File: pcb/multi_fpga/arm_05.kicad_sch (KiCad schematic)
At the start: 16 parts, among them U41 IM72D128V01XTMA1, U42 IM72D128V01XTMA1, U43 IM72D128V01XTMA1, U44 IM72D128V01XTMA1, U45 IM72D128V01XTMA1, U46 IM72D128V01XTMA1, U47 IM72D128V01XTMA1, U48 IM72D128V01XTMA1

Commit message: Fixed library and power issues.
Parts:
- C41, C42, C43, C44, C45, C46, C47, C48: symbol C -> multi_fpga:C
- U41, U42, U43, U44, U45, U46, U47, U48: symbol IM72D128 -> multi_fpga:IM72D128

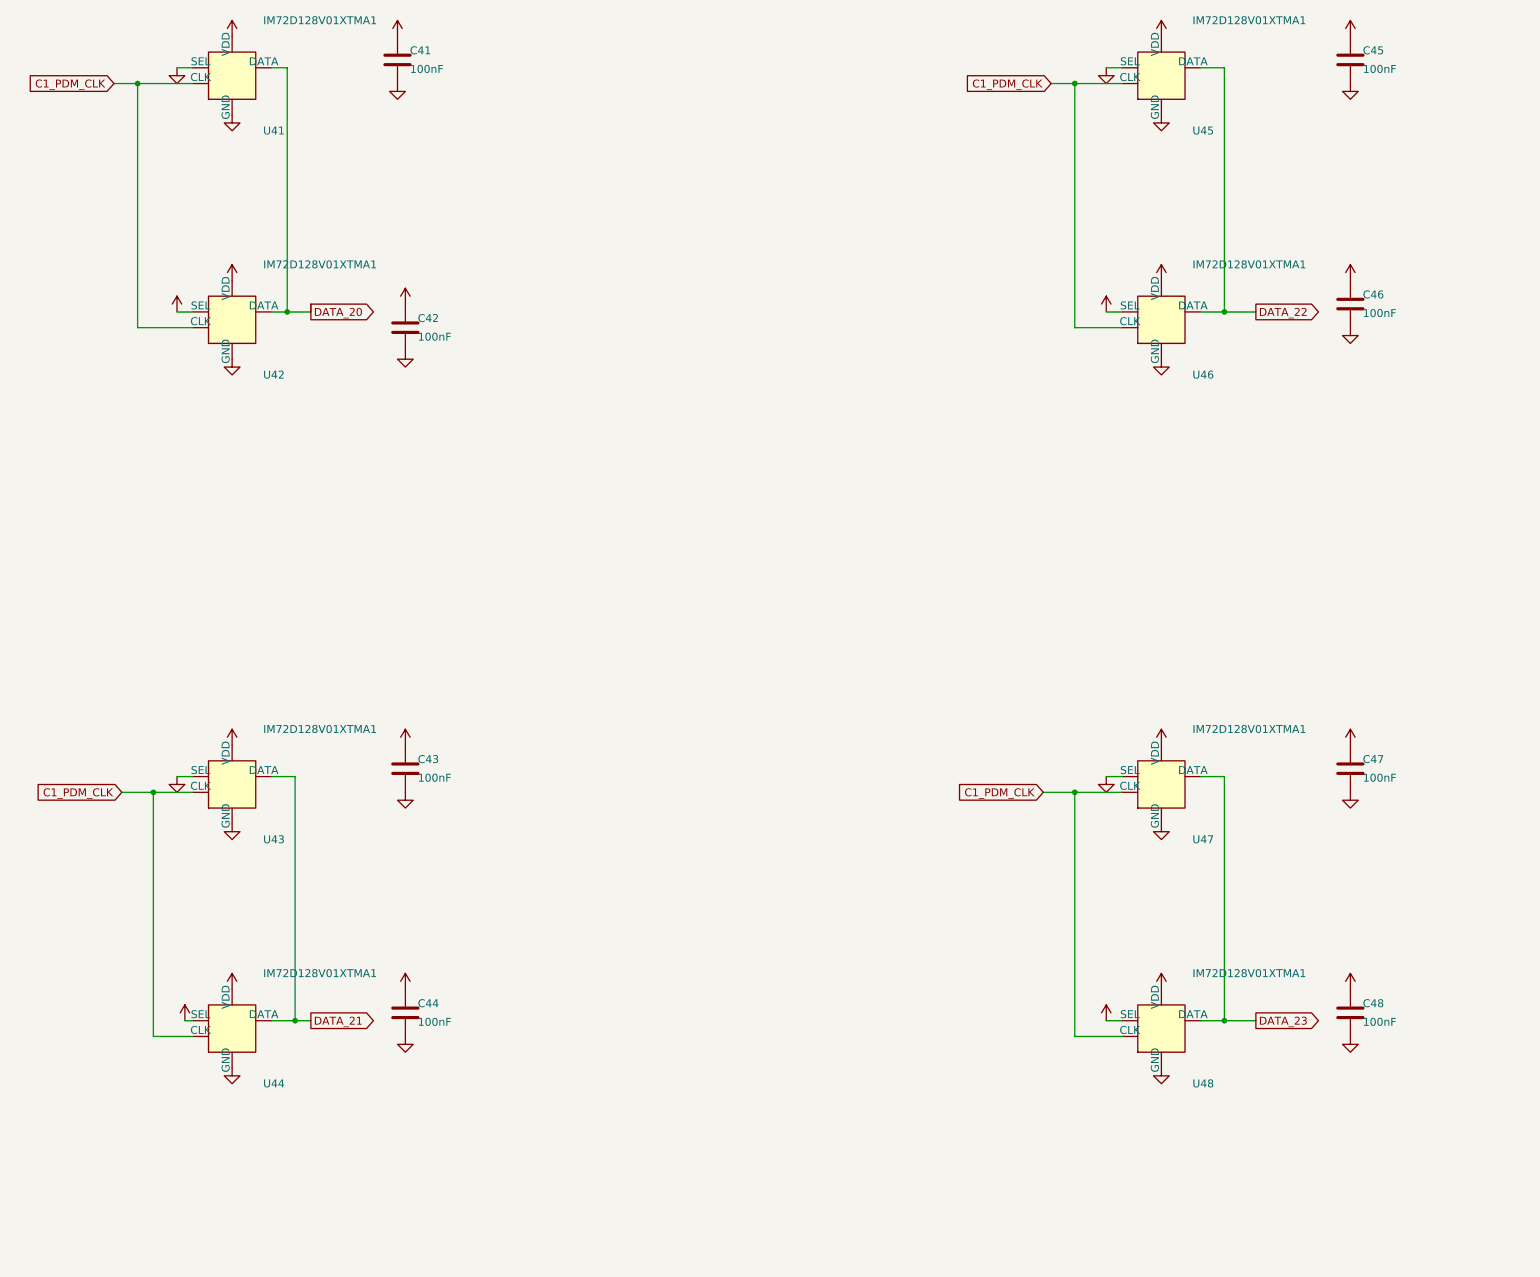
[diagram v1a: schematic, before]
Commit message: Fixed power and C ref des collisions.
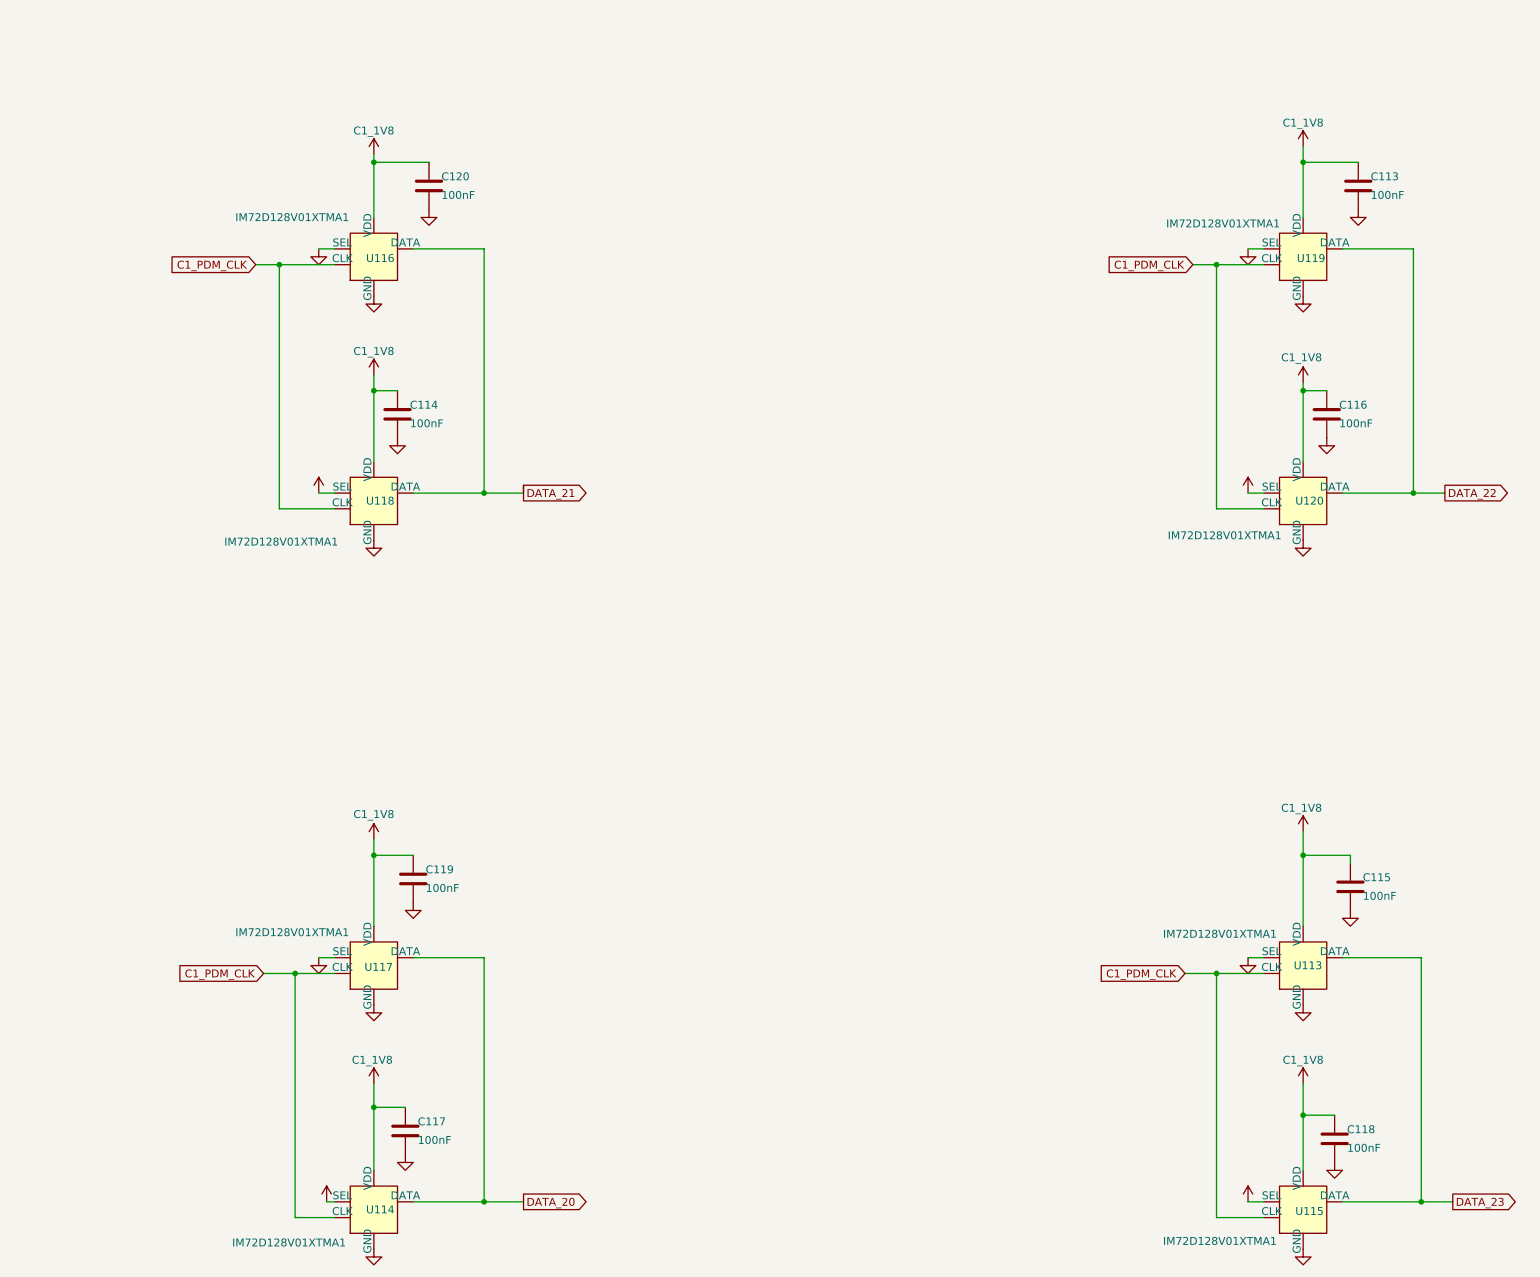
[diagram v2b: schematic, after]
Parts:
- removed C41, C42, C43, C44, C45, C46, C47, C48: 100nF, symbol multi_fpga:C
- removed U41, U42, U43, U44, U45, U46, U47, U48: IM72D128V01XTMA1, symbol multi_fpga:IM72D128
- added C113, C114, C115, C116, C117, C118, C119, C120: 100nF, symbol multi_fpga:C
- added U113, U114, U115, U116, U117, U118, U119, U120: IM72D128V01XTMA1, symbol multi_fpga:IM72D128
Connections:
- net C1_1V8: now also C113.1, C114.1, C115.1, C116.1, C117.1, C118.1, C119.1, C120.1, U113.2 (VDD), U114.2 (VDD), U114.4 (SEL), U115.2 (VDD), U115.4 (SEL), U116.2 (VDD), U117.2 (VDD), U118.2 (VDD), U118.4 (SEL), U119.2 (VDD), U120.2 (VDD), U120.4 (SEL)
- net C1_PDM_CLK: now also U113.3 (CLK), U114.3 (CLK), U115.3 (CLK), U116.3 (CLK), U117.3 (CLK), U118.3 (CLK), U119.3 (CLK), U120.3 (CLK)
- net DATA_20: now also U114.1 (DATA), U117.1 (DATA)
- net DATA_21: now also U116.1 (DATA), U118.1 (DATA)
- net DATA_22: now also U119.1 (DATA), U120.1 (DATA)
- net DATA_23: now also U113.1 (DATA), U115.1 (DATA)
- net GND: now also C113.2, C114.2, C115.2, C116.2, C117.2, C118.2, C119.2, C120.2, U113.4 (SEL), U113.5 (GND), U114.5 (GND), U115.5 (GND), U116.4 (SEL), U116.5 (GND), U117.4 (SEL), U117.5 (GND), U118.5 (GND), U119.4 (SEL), U119.5 (GND), U120.5 (GND)

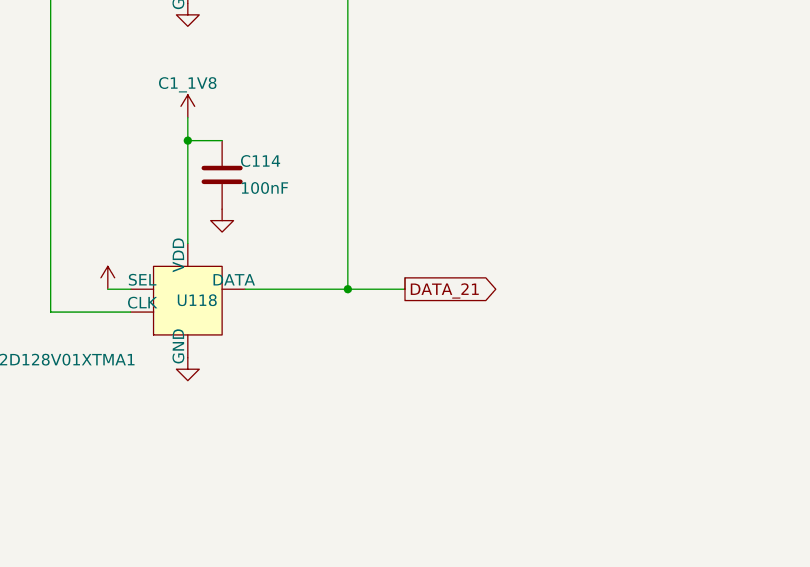
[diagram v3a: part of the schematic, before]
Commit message: Fixed regulator connection errors and dangling wire.
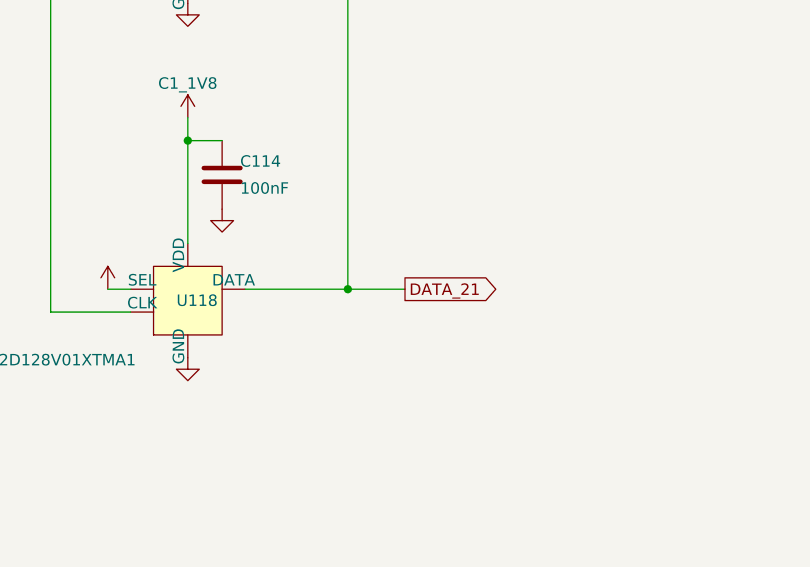
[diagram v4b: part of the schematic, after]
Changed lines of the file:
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@@
-	(wire
-		(pts
-			(xy 127 106.68) (xy 127 107.95)
-		)
-		(stroke
-			(width 0)
-			(type default)
-		)
-	)
 	(wire
 		(pts

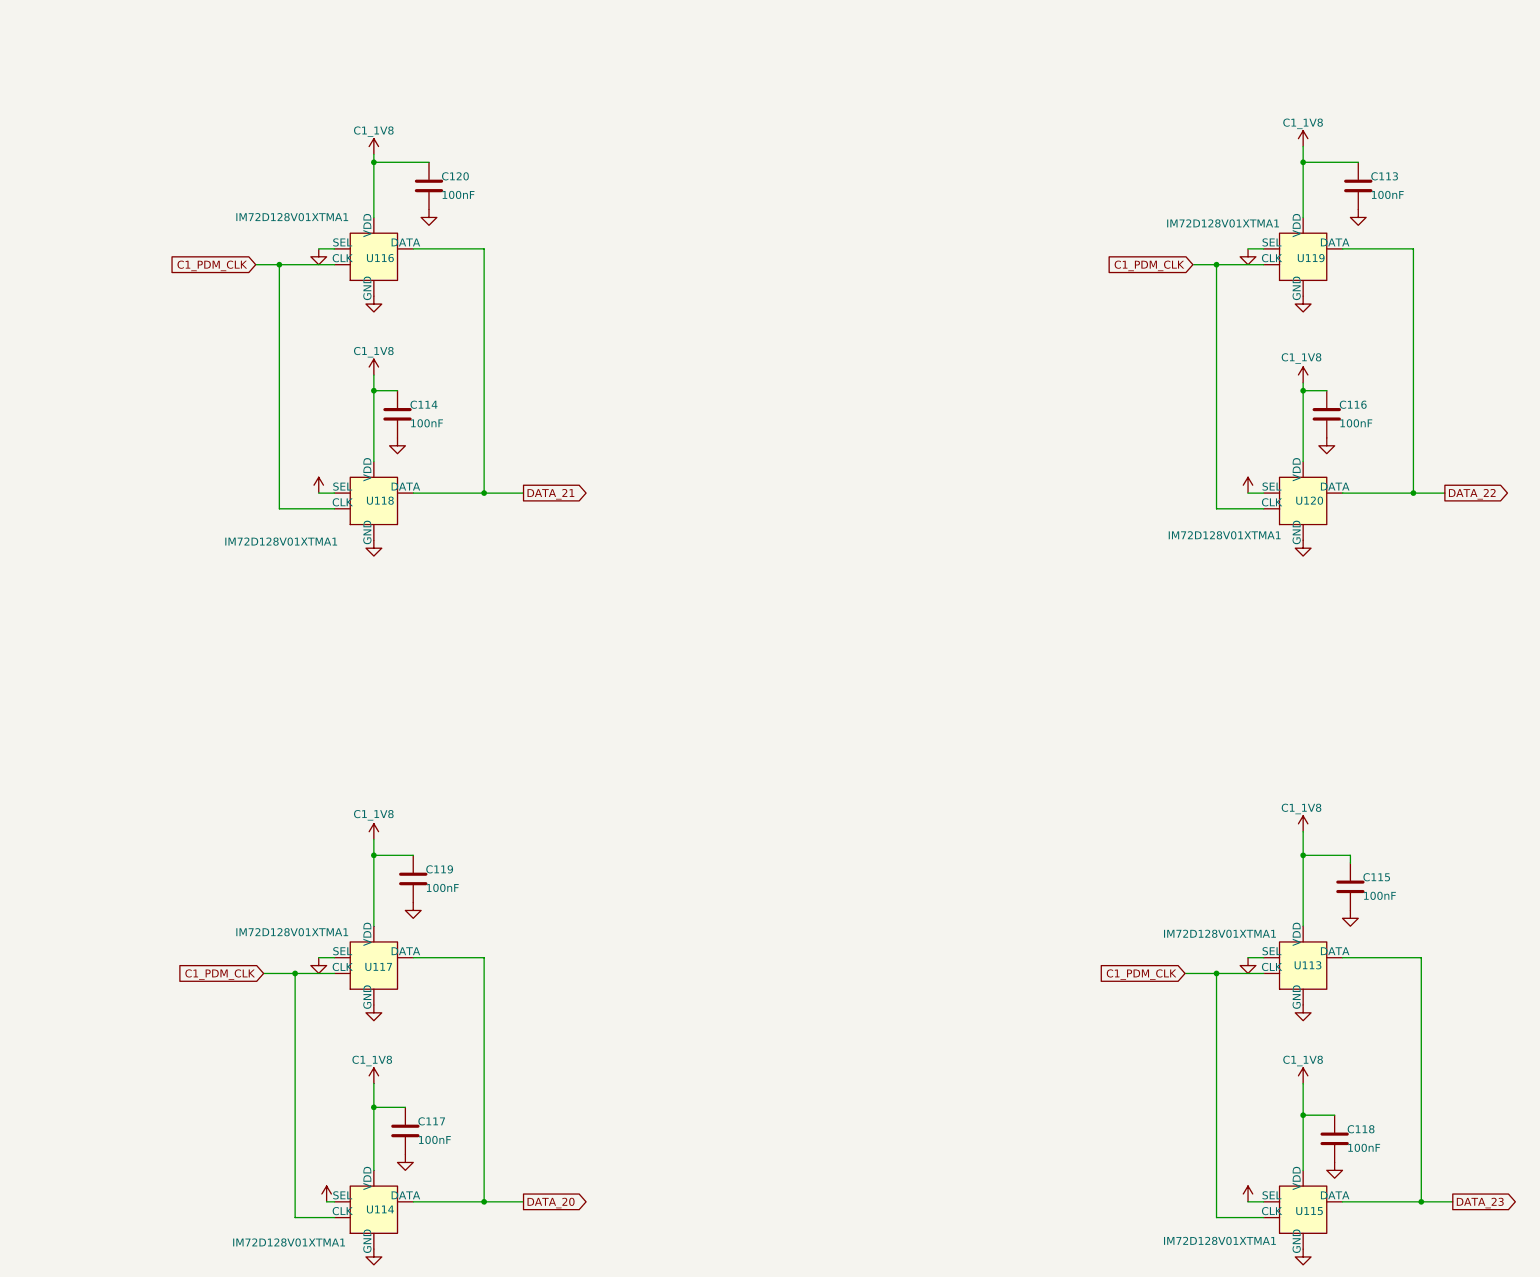
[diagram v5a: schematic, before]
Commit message: Global fix of res defs.
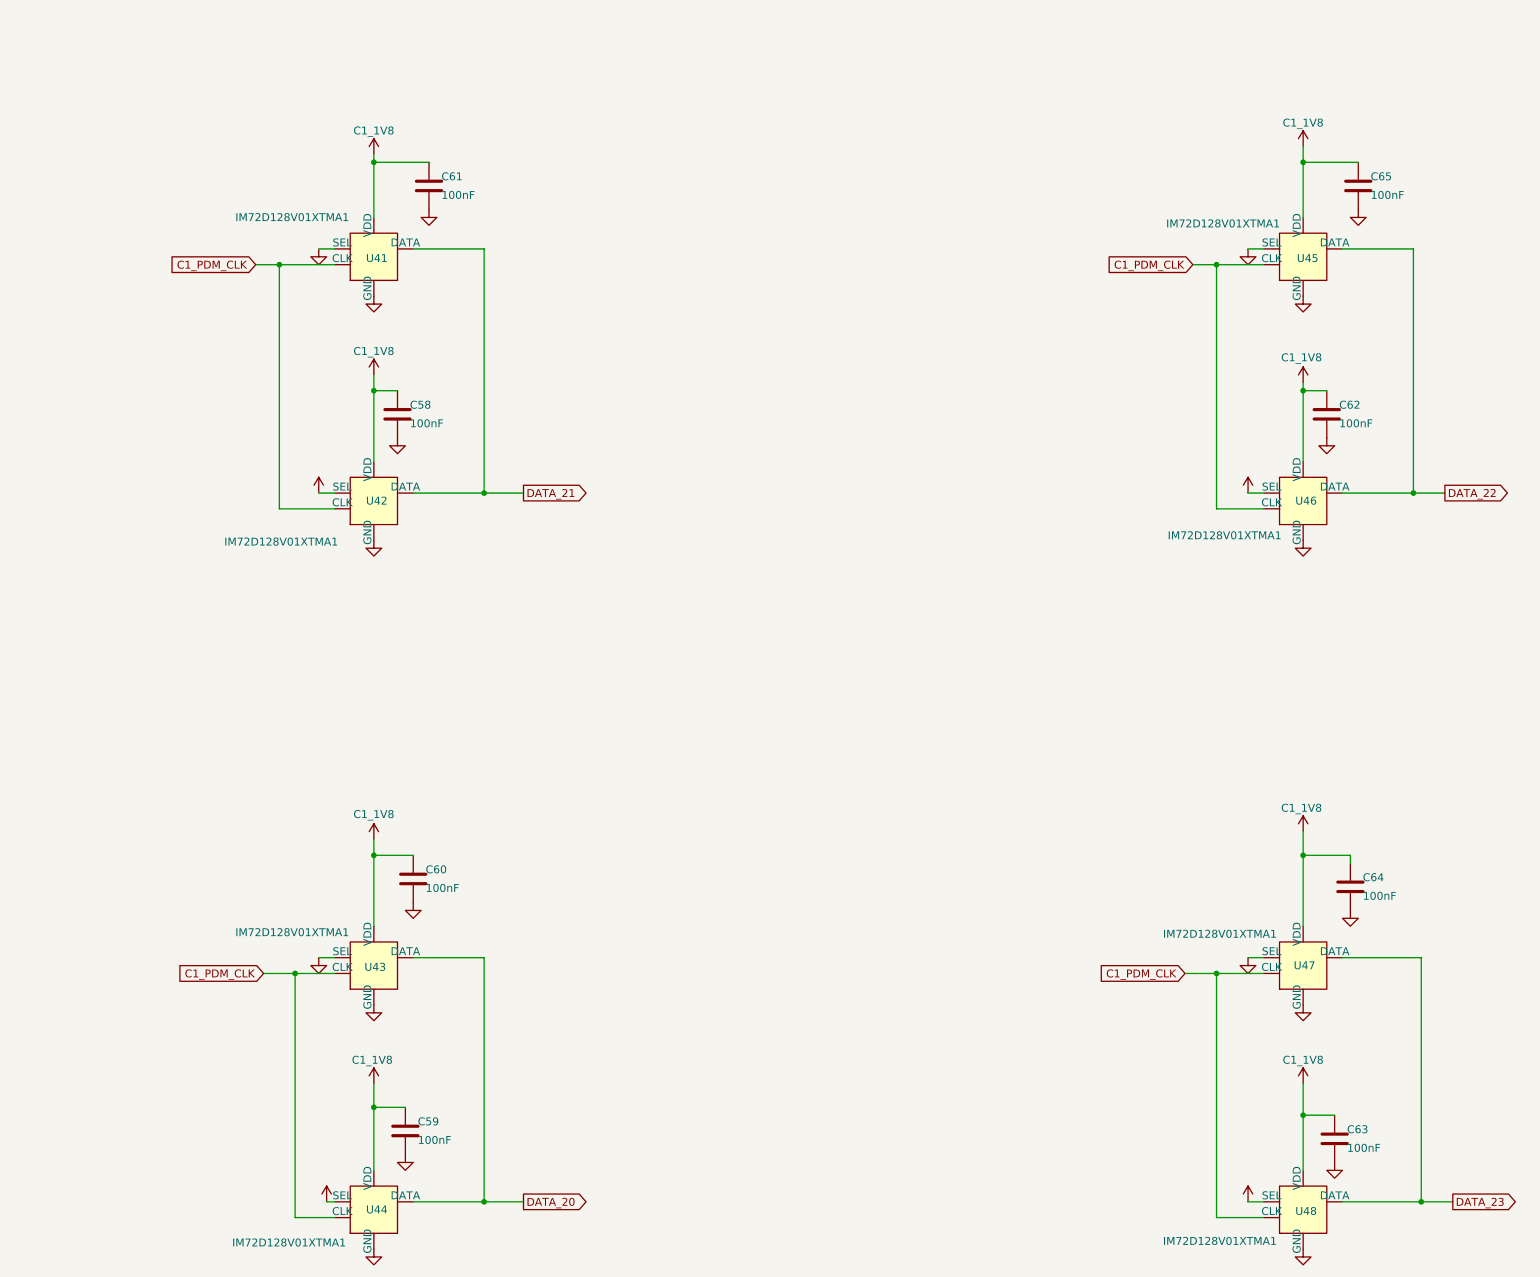
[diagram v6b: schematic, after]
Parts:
- renumbered C114 to C58, C117 to C59, C119 to C60, C120 to C61, C116 to C62, C118 to C63, C115 to C64, C113 to C65, U116 to U41, U118 to U42, U117 to U43, U114 to U44, U119 to U45, U120 to U46, U113 to U47, U115 to U48
